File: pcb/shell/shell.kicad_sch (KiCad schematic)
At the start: 220 parts, among them J1 Conn_01x11, J2 Conn_01x11

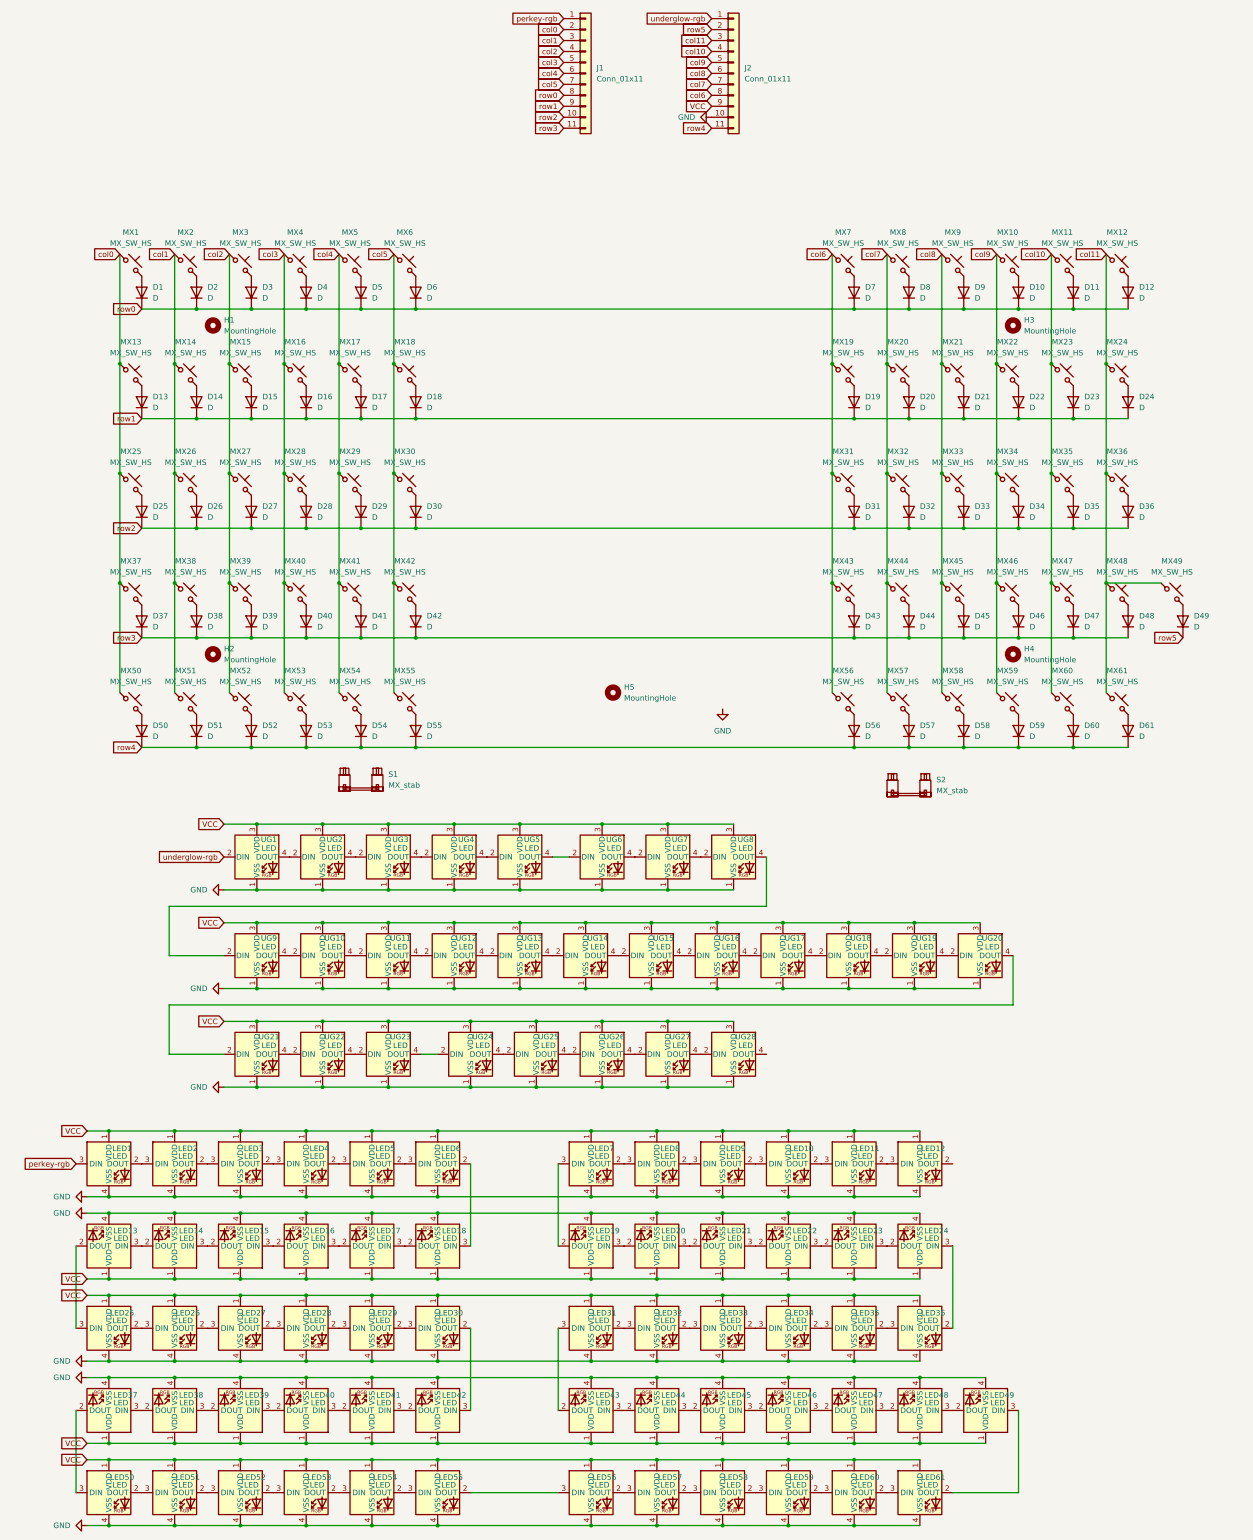
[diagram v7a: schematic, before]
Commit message: added 3x3 core
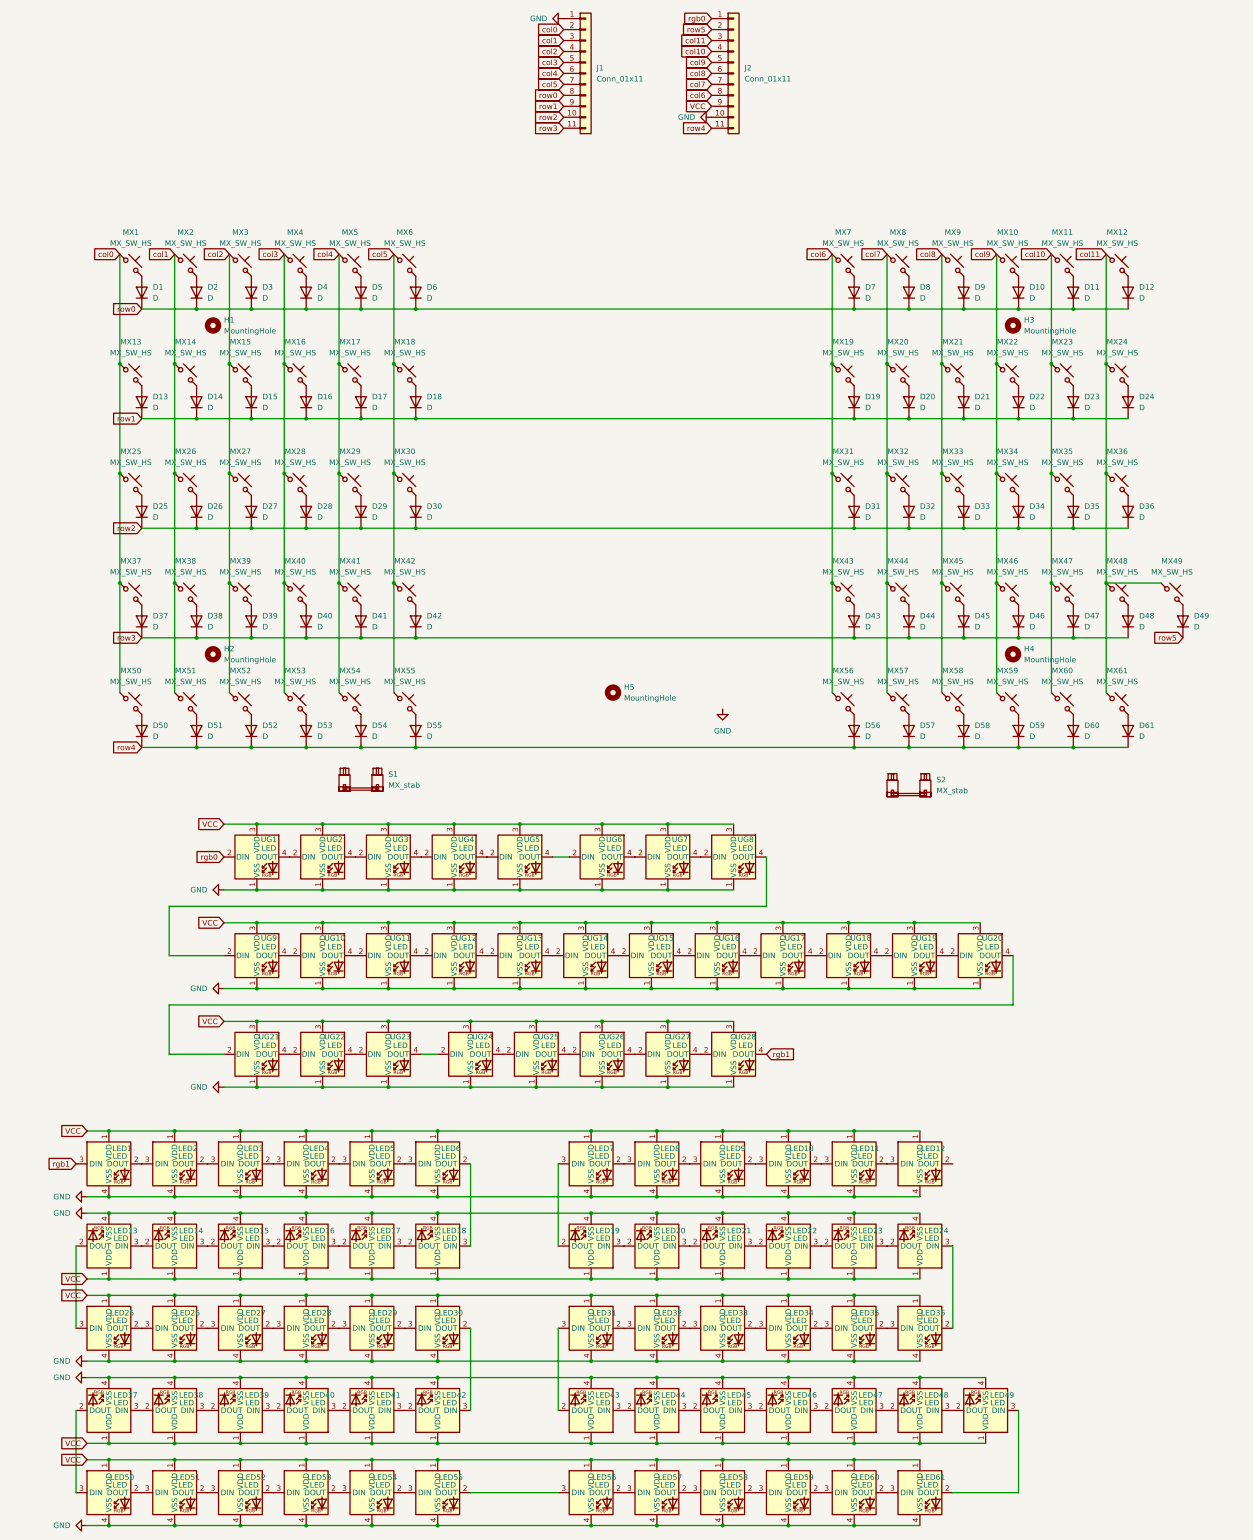
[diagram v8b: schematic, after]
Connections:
- net GND: now also J1.1 (Pin_1)
- net rgb1: now reaches UG28.4 (DOUT)
- net rgb1: now also LED1.3 (DIN)
- removed net perkey-rgb: J1.1 (Pin_1), LED1.3 (DIN)
- net underglow-rgb renamed rgb0
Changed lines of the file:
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@@
 		)
 	)
-	(global_label "row3"
+	(global_label "rgb1"
 		(shape input)
-		(at 128.27 -3.81 180)
+		(at 175.26 210.82 0)
 		(fields_autoplaced yes)
 		(effects
@@
 				(size 1.27 1.27)
 			)
-			(justify right)
+			(justify left)
 		)
 		(property "Intersheetrefs" "${INTERSHEET_REFS}"
-			(at 121.1725 -3.81 0)
+			(at 182.5389 210.82 0)
 			(effects
 				(font
 					(size 1.27 1.27)
 				)
-				(justify right)
+				(justify left)
 				(hide yes)
 			)
 		)
 	)
-	(global_label "perkey-rgb"
+	(global_label "row3"
 		(shape input)
-		(at 128.27 -29.21 180)
+		(at 128.27 -3.81 180)
 		(fields_autoplaced yes)
 		(effects
@@
 		)
 		(property "Intersheetrefs" "${INTERSHEET_REFS}"
-			(at 114.5201 -29.21 0)
+			(at 121.1725 -3.81 0)
 			(effects
 				(font
@@
 		)
 	)
-	(global_label "underglow-rgb"
+	(global_label "rgb0"
+		(shape input)
+		(at 162.56 -29.21 180)
+		(fields_autoplaced yes)
+		(effects
+			(font
+				(size 1.27 1.27)
+			)
+			(justify right)
+		)
+		(property "Intersheetrefs" "${INTERSHEET_REFS}"
+			(at 155.2811 -29.21 0)
+			(effects
+				(font
+					(size 1.27 1.27)
+				)
+				(justify right)
+				(hide yes)
+			)
+		)
+	)
+	(global_label "rgb0"
 		(shape input)
 		(at 49.53 165.1 180)
@@
 		)
 		(property "Intersheetrefs" "${INTERSHEET_REFS}"
-			(at 32.2727 165.1 0)
+			(at 42.2511 165.1 0)
 			(effects
 				(font
@@
 		)
 	)
-	(global_label "perkey-rgb"
+	(global_label "rgb1"
 		(shape input)
 		(at 15.24 236.22 180)
@@
 		)
 		(property "Intersheetrefs" "${INTERSHEET_REFS}"
-			(at 1.4901 236.22 0)
+			(at 7.9611 236.22 0)
 			(effects
 				(font
@@
 		)
 	)
-	(global_label "underglow-rgb"
-		(shape input)
-		(at 162.56 -29.21 180)
-		(fields_autoplaced yes)
-		(effects
-			(font
-				(size 1.27 1.27)
-			)
-			(justify right)
-		)
-		(property "Intersheetrefs" "${INTERSHEET_REFS}"
-			(at 145.3027 -29.21 0)
-			(effects
-				(font
-					(size 1.27 1.27)
-				)
-				(justify right)
-				(hide yes)
-			)
-		)
-	)
 	(global_label "col7"
 		(shape input)
@@
 					(unit 1)
 				)
+			)
+		)
+	)
+	(symbol
+		(lib_id "power:GND")
+		(at 128.27 -29.21 270)
+		(unit 1)
+		(exclude_from_sim no)
+		(in_bom yes)
+		(on_board yes)
+		(dnp no)
+		(fields_autoplaced yes)
+		(property "Reference" "#PWR07"
+			(at 121.92 -29.21 0)
+			(effects
+				(font
+					(size 1.27 1.27)
+				)
+				(hide yes)
+			)
+		)
+		(property "Value" "GND"
+			(at 124.46 -29.2101 90)
+			(effects
+				(font
+					(size 1.27 1.27)
+				)
+				(justify right)
+			)
+		)
+		(property "Footprint" ""
+			(at 128.27 -29.21 0)
+			(effects
+				(font
+					(size 1.27 1.27)
+				)
+				(hide yes)
+			)
+		)
+		(property "Datasheet" ""
+			(at 128.27 -29.21 0)
+			(effects
+				(font
+					(size 1.27 1.27)
+				)
+				(hide yes)
+			)
+		)
+		(property "Description" "Power symbol creates a global label with name \"GND\" , ground"
+			(at 128.27 -29.21 0)
+			(effects
+				(font
+					(size 1.27 1.27)
+				)
+				(hide yes)
+			)
+		)
+		(pin "1"
+		)
+		(instances
+			(project "shell"
+				(path "/e189624d-31ed-4827-8b05-62c0c6e8ce19"
+					(reference "#PWR07")
+					(unit 1)
+				)
